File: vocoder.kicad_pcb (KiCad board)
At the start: 2 copper layers, 49.7 x 38.4 mm, 63 parts, among them J1 AudioJack4, J2 Conn_01x02_Socket, J3 Conn_01x02_Pin, J4 USB_C_Receptacle_USB2.0_16P, Q1 Q_NPN_BCE, Q2 Q_NPN_BCE, Q3 AO3401A, Q4 Q_NPN_BCE, SW1 SW_SPDT, SW2 SW_Push, SW3 SW_Push, U1 ESP32-S3-MINI-1, U3 BQ24074RGT, U4 TPS63031DSK, U5 ADAU1761

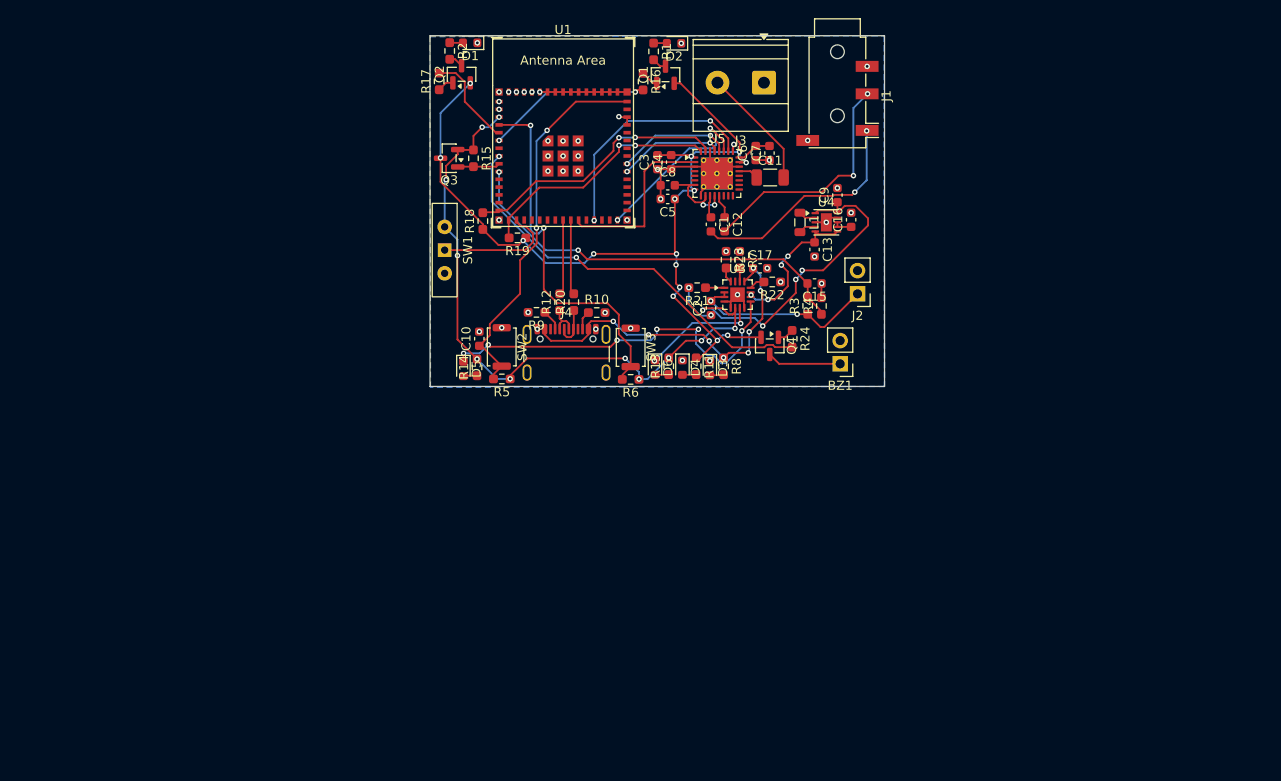
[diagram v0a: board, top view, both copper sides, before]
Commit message: replaced esp32-s3 mini with esp32-s3-wroom, added needed op amp and amp
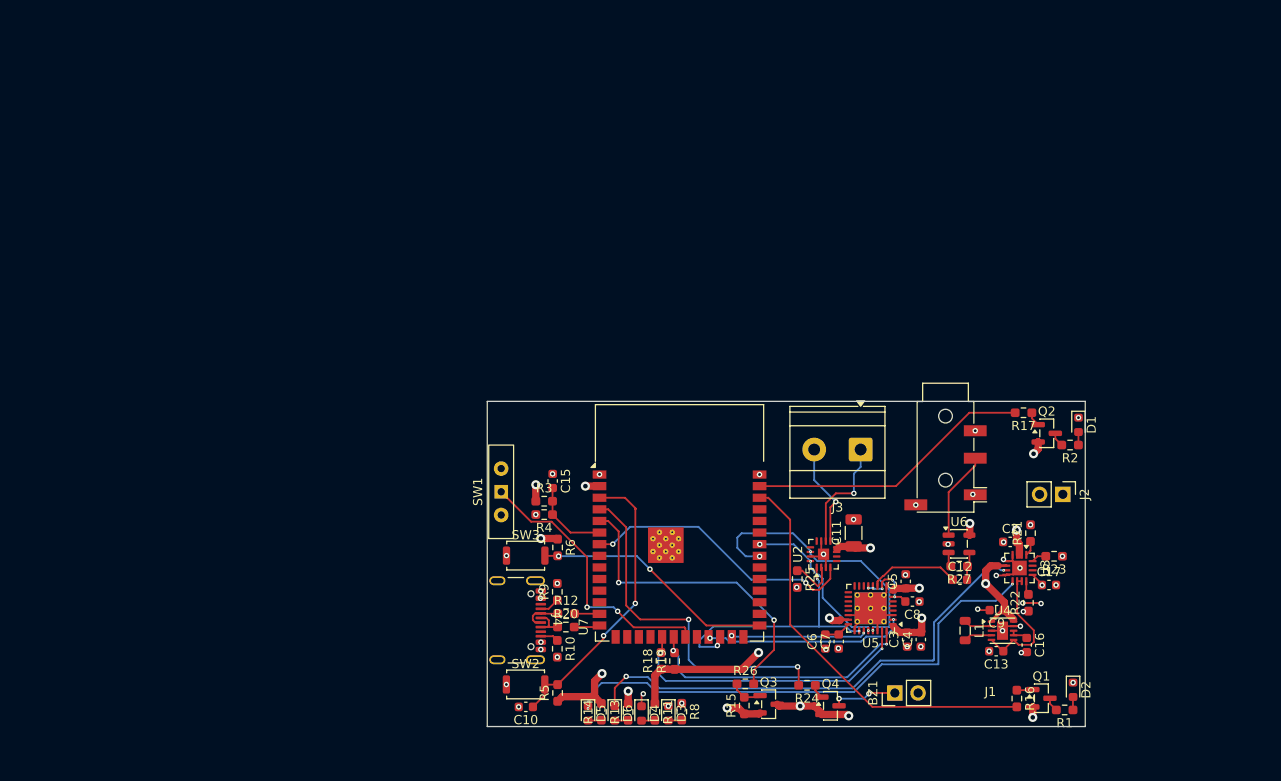
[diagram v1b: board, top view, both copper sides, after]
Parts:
- removed C1: 2.2u, Capacitor_SMD:C_0603_1608Metric
- removed R7: 72k, Resistor_SMD:R_0603_1608Metric_Pad0.98x0.95mm_HandSolder
- removed U1: ESP32-S3-MINI-1, PCM_Espressif:ESP32-S3-MINI-1
- added R25: 100k, Resistor_SMD:R_0603_1608Metric_Pad0.98x0.95mm_HandSolder, F.Cu at (156.9, 86.2)
- added R26: 100, Resistor_SMD:R_0603_1608Metric_Pad0.98x0.95mm_HandSolder, F.Cu at (151.2, 97.7)
- added R27: 51, Resistor_SMD:R_0603_1608Metric_Pad0.98x0.95mm_HandSolder, F.Cu at (174.6, 84.8)
- added U2: MAX98357A, Package_DFN_QFN:TQFN-16-1EP_3x3mm_P0.5mm_EP1.23x1.23mm, F.Cu at (159.8, 83.5)
- added U6: ~, custom_footprints:TLV9041, F.Cu at (174.6, 82.4)
- added U7: ESP32-S3-WROOM-1, RF_Module:ESP32-S3-WROOM-1, F.Cu at (144.0, 80.0)
- C11: value 10u -> 220u
- R1, R2: value 100 -> 1k
- R11, R8: value 220 -> 1k
- R18, R19: value 4.7k -> 10k
- R22, R23: value 910 -> 1k
- moved R1 84.9 mm to (186.1, 100.5), turned to 180 degrees
- moved D2 83.1 mm to (187.1, 98.3), turned to -90 degrees
- moved R2 80.4 mm to (186.7, 71.6), turned to 180 degrees
- moved Q1 79.6 mm to (183.6, 99.2), turned to 0 degrees
- moved R16 78.9 mm to (180.9, 99.3)
- moved D1 78.6 mm to (187.7, 69.3), turned to -90 degrees
- moved Q2 75.1 mm to (184.2, 70.3), turned to 0 degrees
- moved R17 73.5 mm to (181.6, 68.0), turned to 180 degrees
- moved Q3 69.2 mm to (153.8, 99.9), turned to 0 degrees
- moved R15 66.8 mm to (151.1, 100.0), turned to 90 degrees
- moved C3 58.9 mm to (168.9, 92.8)
- moved C4 58.9 mm to (170.4, 92.8)
- moved C6 54.0 mm to (160.0, 93.0)
- moved C7 54.0 mm to (161.4, 93.0)
- moved C8 52.8 mm to (169.5, 88.7), turned to 180 degrees
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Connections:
- net 3V3_SWITCH renamed Net-(Q3-G)
- C11 pad 1: Net-(U5-MONOOUT) -> BATT+
- C11 pad 2: Net-(J3-Pin_2) -> GND
- C12 pad 1: Net-(U5-RINN) -> Net-(U5-LINN)
- J1 pad R1: Net-(C12-Pad2) -> Net-(U6-+)
- J1 pad T: Net-(C1-Pad2) -> GND
- J3 pad 1: GND -> Net-(J3-Pin_1)
- Q3 pad 2: 3V3_PRE -> 3V3
- Q3 pad 3: 3V3 -> 3V3_PRE
- U3 pad 14: Net-(U3-TMR) -> unconnected-(U3-TMR-Pad14)
- U5 pad 13: Net-(U5-RINN) -> CM
- U5 pad 21: Net-(U5-MONOOUT) -> unconnected-(U5-MONOOUT-Pad21)
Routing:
- net BATT+: track 20.9 -> 73.9 mm, vias 2 -> 3
- net USB_5V: track 39.0 -> 88.1 mm, vias 8 -> 6
- net Net-(D6-K): track 13.0 -> 53.8 mm
- net 3V3_PRE: track 106.0 -> 145.5 mm, vias 15 -> 6
- net BATT_READ: track 44.9 -> 8.86 mm, vias 2 -> 0
- net 3V3: track 99.7 -> 135.1 mm, vias 15 -> 9
- net 3V3_SWITCH: track 0.00 -> 34.7 mm, vias 0 -> 2
- net AMP_SWITCH: track 0.00 -> 30.6 mm, vias 0 -> 2
- net LED_RIGHT: track 18.0 -> 44.3 mm, vias 2 -> 0
- net Net-(C1-Pad2): track 25.4 -> 0.00 mm, vias 2 -> 0
- net Net-(C12-Pad2): track 26.2 -> 3.09 mm, vias 2 -> 0
- net LED_LEFT: track 10.5 -> 31.3 mm
- net I2S_LRCLK: track 11.5 -> 29.9 mm, vias 2 -> 3
- net SWITCH_INPUT: track 13.5 -> 30.5 mm, vias 0 -> 2
- net Net-(D5-K): track 41.9 -> 56.8 mm, vias 6 -> 2
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- added copper zone on In1.Cu, net GND
- removed copper zone on B.Cu, net GND
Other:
- board size 49.7 x 38.4 mm -> 65.4 x 35.6 mm
- copper layers 2 -> 4

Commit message: semi working before removing battery and adding necessary changes
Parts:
- removed BZ1: Buzzer, Connector_PinHeader_2.54mm:PinHeader_1x02_P2.54mm_Vertical
- removed C11: 220u, Capacitor_SMD:C_1206_3216Metric
- removed C12: 2.2u, Capacitor_SMD:C_0603_1608Metric
- removed C13, C17, C9: 10u, Capacitor_SMD:C_0603_1608Metric
- removed C15: 100n, Capacitor_SMD:C_0603_1608Metric
- removed C16: 0.1u, Capacitor_SMD:C_0603_1608Metric
- removed D2: LED RED, LED_SMD:LED_0603_1608Metric
- removed J3: Conn_01x02_Pin, TerminalBlock_Phoenix:TerminalBlock_Phoenix_MKDS-1,5-2-5.08_1x02_P5.08mm_Horizontal
- removed L1: 1.5uH, Inductor_SMD:L_0805_2012Metric
- removed Q1, Q2, Q4: Q_NPN_BCE, Package_TO_SOT_SMD:SOT-23
- removed R18, R19: 10k, Resistor_SMD:R_0603_1608Metric_Pad0.98x0.95mm_HandSolder
- removed R22, R24: 1k, Resistor_SMD:R_0603_1608Metric_Pad0.98x0.95mm_HandSolder
- removed R25: 100k, Resistor_SMD:R_0603_1608Metric_Pad0.98x0.95mm_HandSolder
- removed R26: 100, Resistor_SMD:R_0603_1608Metric_Pad0.98x0.95mm_HandSolder
- removed R27: 51, Resistor_SMD:R_0603_1608Metric_Pad0.98x0.95mm_HandSolder
- removed U5: ADAU1761, Package_CSP:LFCSP-32-1EP_5x5mm_P0.5mm_EP3.5x3.5mm_ThermalVias
- removed U6: ~, custom_footprints:TLV9041
- added C1: 1u, Capacitor_SMD:C_0603_1608Metric, F.Cu at (169.6, 101.6)
- added J5: Conn_02x03_Top_Bottom, Connector_PinHeader_2.54mm:PinHeader_2x03_P2.54mm_Vertical, F.Cu at (205.5, 90.0)
- added LS1: Speaker, TerminalBlock_Phoenix:TerminalBlock_Phoenix_MKDS-1,5-2-5.08_1x02_P5.08mm_Horizontal, F.Cu at (194.2, 76.8)
- added R7: 10k, Resistor_SMD:R_0603_1608Metric_Pad0.98x0.95mm_HandSolder, F.Cu at (160.9, 82.4)
- added SW4: RotaryEncoder_Switch, Rotary_Encoder:RotaryEncoder_Bourns_Horizontal_PEC12R-2x17F-Sxxxx, F.Cu at (202.7, 100.2)
- added U1: MCP73831-2-MC, Package_DFN_QFN:DFN-8-1EP_3x2mm_P0.5mm_EP1.7x1.4mm, F.Cu at (177.9, 98.8)
- C2, C8: value 10u -> 1u
- C3, C6: value 100n -> 1u
- C4, C7: footprint Capacitor_SMD:C_0603_1608Metric -> Capacitor_SMD:C_0805_2012Metric
- C5: value 100n -> 10u; footprint Capacitor_SMD:C_0603_1608Metric -> Capacitor_SMD:C_0805_2012Metric
- D1: value LED RED -> SS34; footprint LED_SMD:LED_0603_1608Metric -> Diode_SMD:D_SOD-123
- D3: value LED BLUE -> SS34; footprint LED_SMD:LED_0603_1608Metric -> Diode_SMD:D_SOD-123
- D4: value LED GREEN -> SS34; footprint LED_SMD:LED_0603_1608Metric -> Diode_SMD:D_SOD-123
- D5: value LED RED -> 1N4148; footprint LED_SMD:LED_0603_1608Metric -> Diode_SMD:D_SOD-323
- D6: value LED GREEN -> 1N4148; footprint LED_SMD:LED_0603_1608Metric -> Diode_SMD:D_SOD-323
- J1: value AudioJack4 -> Micro_SD_Card_Det1; footprint Connector_Audio:Jack_3.5mm_PJ320D_Horizontal -> MyAntenna_manufacturer:Untitled
- R1, R11, R13, R14, R16, R17, R23, R8: value 1k -> 10k
- R2: value 1k -> 2.2k
- R3, R4: value 100k -> 470k
- SW1: value SW_SPDT -> SW_Push; footprint Button_Switch_THT:SW_Slide-03_Wuerth-WS-SLTV_10x2.5x6.4_P2.54mm -> Button_Switch_SMD:Panasonic_EVQPUJ_EVQPUA
- SW2, SW3: footprint Button_Switch_SMD:SW_Push_SPST_NO_Alps_SKRK -> Button_Switch_SMD:SW_SPST_TS-1088-xR020
- U2: value MAX98357A -> AP2112K-3.3; footprint Package_DFN_QFN:TQFN-16-1EP_3x3mm_P0.5mm_EP1.23x1.23mm -> Package_TO_SOT_SMD:SOT-23-5
- U3: value BQ24074RGT -> MAX98357A; footprint Package_DFN_QFN:VQFN-16-1EP_3x3mm_P0.5mm_EP1.6x1.6mm -> Package_DFN_QFN:TQFN-16-1EP_3x3mm_P0.5mm_EP1.23x1.23mm
- U4: value TPS63031DSK -> MAX40200AUK; footprint Package_SON:WSON-10-1EP_2.5x2.5mm_P0.5mm_EP1.2x2mm -> Package_TO_SOT_SMD:SOT-23-5
- U7: footprint RF_Module:ESP32-S3-WROOM-1 -> RF_Module:ESP32-S3-WROOM-1U
- moved SW1 78.1 mm to (202.5, 73.3), turned to 0 degrees
- moved D4 60.2 mm to (198.4, 86.7), turned to 0 degrees
- moved D3 58.0 mm to (198.4, 84.5), turned to 0 degrees
- moved D1 40.7 mm to (159.6, 98.8), turned to 180 degrees
- moved C6 35.1 mm to (194.5, 86.5), turned to -90 degrees
- moved R14 35.1 mm to (160.9, 76.5), turned to 0 degrees
- moved U7 32.1 mm to (176.1, 81.8)
- moved R13 32.0 mm to (160.9, 78.0), turned to 0 degrees
- moved R4 31.5 mm to (160.0, 86.0)
- moved R3 31.5 mm to (160.0, 84.5)
- moved R2 31.3 mm to (175.6, 100.8)
- moved R17 30.8 mm to (188.7, 98.0), turned to 0 degrees
- moved D5 29.9 mm to (163.5, 95.9)
- moved R11 28.9 mm to (160.9, 79.4), turned to 0 degrees
- moved R23 26.4 mm to (160.4, 93.3), turned to 0 degrees
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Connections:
- C2 pad 1: GND -> 3V3
- C2 pad 2: BATT+ -> GND
- C3 pad 2: 3V3 -> USB_5V
- C4 pad 1: GND -> USB_5V
- C4 pad 2: 3V3 -> GND
- C5 pad 1: 3V3 -> GND
- C5 pad 2: GND -> BATT+
- C6 pad 1: GND -> Net-(D3-K)
- C6 pad 2: Net-(U5-DVDDOUT) -> GND
- C7 pad 2: Net-(U5-DVDDOUT) -> 3V3
- C8 pad 1: GND -> 3V3
- C8 pad 2: CM -> GND
- D1 pad 1: GND -> Net-(D1-K)
- D1 pad 2: Net-(D1-A) -> USB_5V
- D3 pad 1: GND -> Net-(D3-K)
- D3 pad 2: Net-(D3-A) -> USB_5V
- D4 pad 1: GND -> Net-(D3-K)
- D4 pad 2: Net-(D4-A) -> AMP_POWER
- D5 pad 1: Net-(D5-K) -> POWER_SWITCH
- D6 pad 1: Net-(D6-K) -> BUTTON_READ
- D6 pad 2: Net-(D6-A) -> Net-(D5-A)
- Q3 pad 1: Net-(Q3-G) -> Net-(D5-A)
- Q3 pad 2: 3V3 -> Net-(D1-K)
- Q3 pad 3: 3V3_PRE -> AMP_POWER
- R1 pad 1: Net-(D2-A) -> AMP_SWITCH
- R1 pad 2: Net-(Q1-E) -> GND
- R11 pad 2: Net-(D4-A) -> CMD
- R13 pad 1: Net-(D6-A) -> 3V3
- R13 pad 2: 3V3_PRE -> D0
- R14 pad 1: Net-(D5-A) -> 3V3
- R14 pad 2: 3V3_PRE -> D1
- R15 pad 1: 3V3_PRE -> Net-(D5-A)
- R15 pad 2: Net-(Q3-G) -> Net-(D1-K)
- R16 pad 1: Net-(Q1-B) -> 3V3
- R16 pad 2: LED_RIGHT -> ENC_LEFT
- R17 pad 1: Net-(Q2-B) -> 3V3
- R17 pad 2: LED_LEFT -> ENC_RIGHT
- R2 pad 1: Net-(D1-A) -> Net-(U1-PROG)
- R2 pad 2: Net-(Q2-E) -> GND
- R21 pad 1: Net-(U3-TS) -> 3V3
- R21 pad 2: GND -> ENC_PUSH
- R23 pad 1: GND -> 3V3
- R23 pad 2: Net-(U3-ISET) -> BUTTON_READ
- R5 pad 1: 3V3_PRE -> 3V3
- R6 pad 1: 3V3_PRE -> 3V3
- R8 pad 1: USB_5V -> 3V3
- R8 pad 2: Net-(D3-A) -> D3
- SW1 pad 1: SWITCH_INPUT -> BUTTON_READ
- SW1 pad 2: 3V3_PRE -> GND
- U2 pad 1: I2S_DATA_OUT -> AMP_POWER
- U2 pad 2: Net-(U2-GAIN_SLOT) -> GND
- U2 pad 3: GND -> AMP_POWER
- U2 pad 4: AMP_SWITCH -> unconnected-(U2-NC-Pad4)
- U2 pad 5: unconnected-(U2-NC-Pad5) -> 3V3
- U3 pad 1: Net-(U3-TS) -> I2S_DATA_OUT
- U3 pad 10: Net-(U4-EN) -> Net-(U3-OUTN)
- U3 pad 11: Net-(U4-EN) -> GND
- U3 pad 12: Net-(U3-ILIM) -> unconnected-(U3-NC-Pad12)
- U3 pad 13: USB_5V -> unconnected-(U3-NC-Pad13)
- U3 pad 14: unconnected-(U3-TMR-Pad14) -> I2S_LRCLK
- U3 pad 15: unconnected-(U3-ITERM-Pad15) -> GND
- U3 pad 16: Net-(U3-ISET) -> I2S_BCLK
- U3 pad 2: BATT+ -> GND
- U3 pad 3: BATT+ -> GND
- U3 pad 4: GND -> AMP_SWITCH
- U3 pad 5: GND -> unconnected-(U3-NC-Pad5)
- U3 pad 6: 3V3_PRE -> unconnected-(U3-NC-Pad6)
- U3 pad 7: Net-(D6-K) -> Net-(D3-K)
- U3 pad 8: GND -> Net-(D3-K)
- U3 pad 9: Net-(D5-K) -> Net-(U3-OUTP)
- U4 pad 1: 3V3_PRE -> BATT+
- U4 pad 2: Net-(U4-L2) -> GND
- U4 pad 3: GND -> BATT+
- U4 pad 4: Net-(U4-L1) -> unconnected-(U4-NC-Pad4)
- U4 pad 5: Net-(U4-EN) -> Net-(D1-K)
- U7 pad 10: unconnected-(U7-IO17-Pad10) -> BATT_READ
- U7 pad 11: unconnected-(U7-IO18-Pad11) -> POWER_SWITCH
- U7 pad 19: SDA -> CHARGE_STATUS
- U7 pad 2: 3V3_PRE -> 3V3
- U7 pad 20: SCL -> unconnected-(U7-IO12-Pad20)
- U7 pad 21: SWITCH_INPUT -> BUTTON_READ
- U7 pad 22: unconnected-(U7-IO14-Pad22) -> DET
- U7 pad 23: I2S_MCLK -> ENC_LEFT
- U7 pad 24: I2S_DATA_OUT -> ENC_PUSH
- U7 pad 25: I2S_DATA_IN -> ENC_RIGHT
- U7 pad 31: unconnected-(U7-IO38-Pad31) -> AMP_SWITCH
- U7 pad 32: unconnected-(U7-IO39-Pad32) -> I2S_DATA_OUT
- U7 pad 33: I2S_LRCLK -> I2S_BCLK
- U7 pad 34: I2S_BCLK -> I2S_LRCLK
- U7 pad 38: LED_RIGHT -> I2S_MCLK
- U7 pad 39: LED_LEFT -> I2S_DATA_IN
- U7 pad 4: BUZZER -> D1
- U7 pad 5: 3V3_SWITCH -> D0
- U7 pad 6: BATT_READ -> CLK
- U7 pad 7: AMP_SWITCH -> CMD
- U7 pad 8: unconnected-(U7-IO15-Pad8) -> D3
- U7 pad 9: unconnected-(U7-IO16-Pad9) -> D2
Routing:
- net 3V3_PRE: track 145.5 -> 0.00 mm, vias 6 -> 0
- net BUTTON_READ: track 0.00 -> 69.1 mm, vias 0 -> 3
- net Net-(D5-K): track 56.8 -> 0.00 mm, vias 2 -> 0
- net Net-(D6-K): track 53.8 -> 0.00 mm, vias 2 -> 0
- net AMP_POWER: track 0.00 -> 47.7 mm, vias 0 -> 2
- net LED_RIGHT: track 44.3 -> 0.00 mm
- net BUZZER: track 38.5 -> 0.00 mm, vias 2 -> 0
- net DET: track 0.00 -> 35.2 mm, vias 0 -> 2
- net 3V3_SWITCH: track 34.7 -> 0.00 mm, vias 2 -> 0
- net SDA: track 32.4 -> 0.00 mm, vias 2 -> 0
- net ENC_LEFT: track 0.00 -> 31.9 mm
- net LED_LEFT: track 31.3 -> 0.00 mm
- net SCL: track 30.5 -> 0.00 mm, vias 2 -> 0
- net SWITCH_INPUT: track 30.5 -> 0.00 mm, vias 2 -> 0
- net ENC_RIGHT: track 0.00 -> 25.4 mm
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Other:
- board size 65.4 x 35.6 mm -> 66 x 34.8 mm

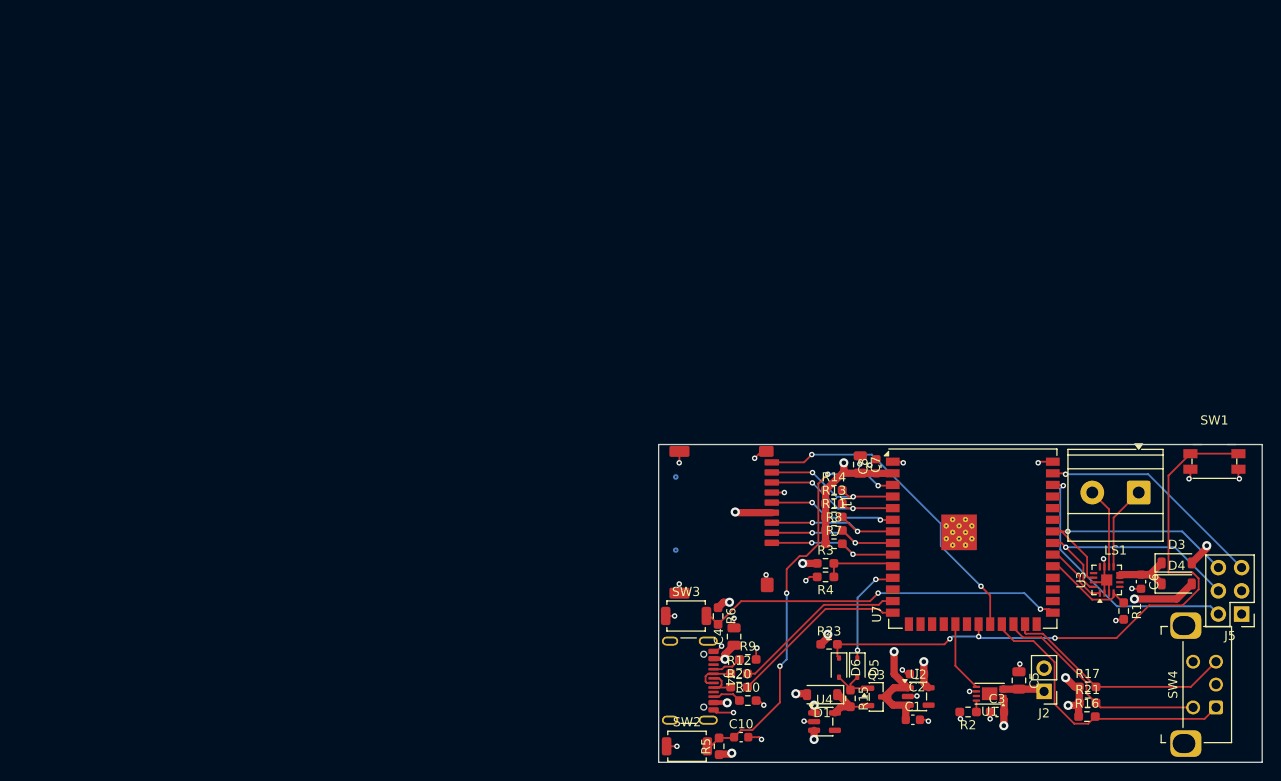
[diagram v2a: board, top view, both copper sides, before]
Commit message: reduced board size, removed BMS, will be powered externally only, fixed I2S wiring
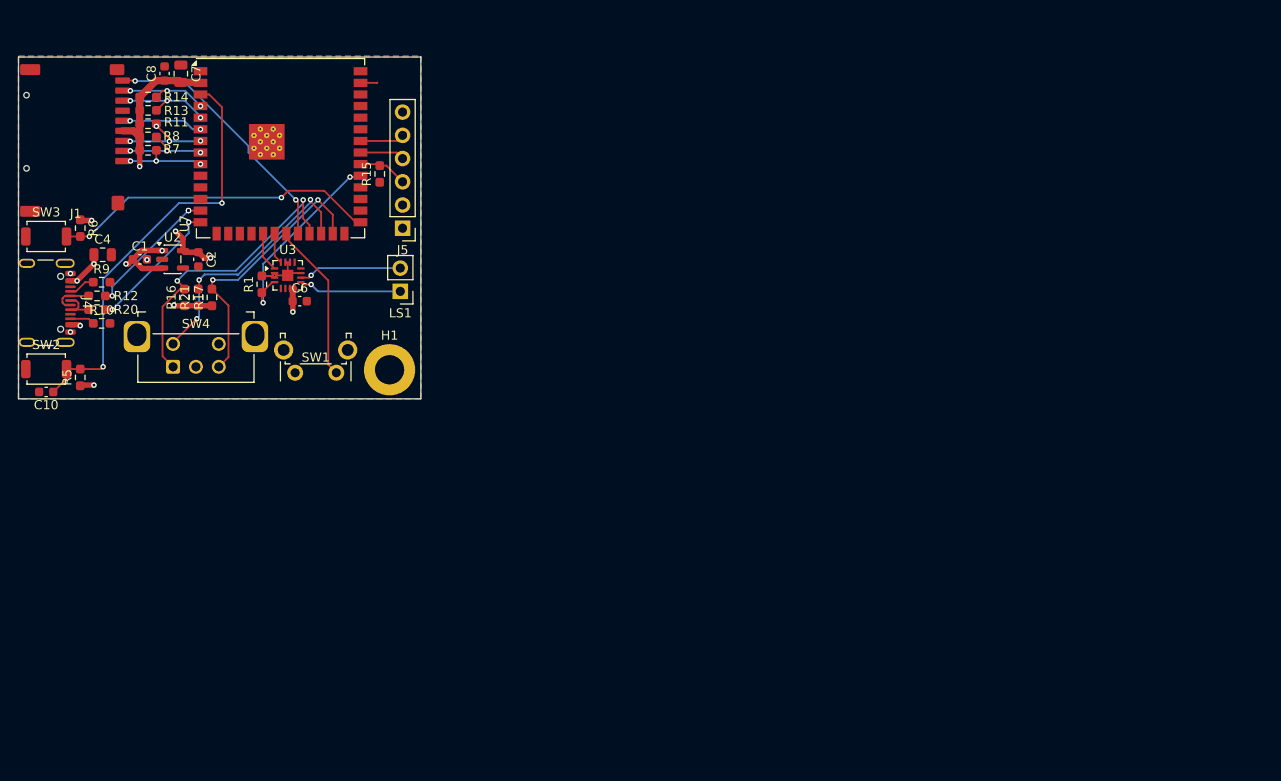
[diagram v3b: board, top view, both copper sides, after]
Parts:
- removed C3: 1u, Capacitor_SMD:C_0603_1608Metric
- removed C5: 10u, Capacitor_SMD:C_0805_2012Metric
- removed D1, D3, D4: SS34, Diode_SMD:D_SOD-123
- removed D5, D6: 1N4148, Diode_SMD:D_SOD-323
- removed J2: Conn_01x02_Socket, Connector_PinHeader_2.54mm:PinHeader_1x02_P2.54mm_Vertical
- removed Q3: AO3401A, Package_TO_SOT_SMD:SOT-23
- removed R2: 2.2k, Resistor_SMD:R_0603_1608Metric_Pad0.98x0.95mm_HandSolder
- removed R23: 10k, Resistor_SMD:R_0603_1608Metric_Pad0.98x0.95mm_HandSolder
- removed R3, R4: 470k, Resistor_SMD:R_0603_1608Metric_Pad0.98x0.95mm_HandSolder
- removed U1: MCP73831-2-MC, Package_DFN_QFN:DFN-8-1EP_3x2mm_P0.5mm_EP1.7x1.4mm
- removed U4: MAX40200AUK, Package_TO_SOT_SMD:SOT-23-5
- added H1: MountingHole_Pad, MountingHole:MountingHole_3.2mm_M3_DIN965_Pad, F.Cu at (112.3, 63.3)
- J5: footprint Connector_PinHeader_2.54mm:PinHeader_2x03_P2.54mm_Vertical -> Connector_PinHeader_2.54mm:PinHeader_1x06_P2.54mm_Vertical
- LS1: footprint TerminalBlock_Phoenix:TerminalBlock_Phoenix_MKDS-1,5-2-5.08_1x02_P5.08mm_Horizontal -> Connector_PinHeader_2.54mm:PinHeader_1x02_P2.54mm_Vertical
- SW1: footprint Button_Switch_SMD:Panasonic_EVQPUJ_EVQPUA -> Button_Switch_THT:SW_Tactile_SPST_Angled_PTS645Vx58-2LFS
- moved SW4 120.0 mm to (88.7, 63.0), turned to 90 degrees
- moved R16 108.8 mm to (89.9, 55.4), turned to 90 degrees
- moved R21 106.9 mm to (91.4, 55.4), turned to 90 degrees
- moved R17 104.8 mm to (92.9, 55.4), turned to 90 degrees
- moved J5 101.0 mm to (113.8, 47.9)
- moved R1 100.8 mm to (98.4, 54.0), turned to 90 degrees
- moved C1 98.4 mm to (85.0, 51.2)
- moved C6 97.0 mm to (102.5, 55.8), turned to 0 degrees
- moved SW1 96.5 mm to (106.5, 63.6), turned to 180 degrees
- moved U3 95.6 mm to (101.2, 53.0), turned to 0 degrees
- moved U2 94.5 mm to (88.6, 51.2)
- moved C2 90.7 mm to (91.4, 51.2), turned to -90 degrees
- moved C8 88.9 mm to (87.7, 30.9)
- moved U7 86.9 mm to (100.4, 39.1)
- moved R7 86.5 mm to (85.9, 39.3)
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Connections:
- C1 pad 1: AMP_POWER -> USB_5V
- C6 pad 1: Net-(D3-K) -> USB_5V
- J5 pad 1: 3V3 -> GND
- J5 pad 2: I2S_MCLK -> 3V3
- J5 pad 3: GND -> I2S_DATA_IN
- J5 pad 4: I2S_BCLK -> I2S_BCLK_MIC
- J5 pad 5: I2S_DATA_IN -> I2S_WS
- J5 pad 6: I2S_LRCLK -> GND
- R15 pad 1: Net-(D5-A) -> GND
- R15 pad 2: Net-(D1-K) -> I2S_DATA_IN
- U2 pad 1: AMP_POWER -> USB_5V
- U2 pad 3: AMP_POWER -> USB_5V
- U3 pad 14: I2S_LRCLK -> GND
- U3 pad 16: I2S_BCLK -> I2S_BCLK_SPEAKER
- U3 pad 7: Net-(D3-K) -> USB_5V
- U3 pad 8: Net-(D3-K) -> USB_5V
- U7 pad 10: BATT_READ -> unconnected-(U7-IO17-Pad10)
- U7 pad 11: POWER_SWITCH -> unconnected-(U7-IO18-Pad11)
- U7 pad 19: CHARGE_STATUS -> I2S_DATA_OUT
- U7 pad 20: unconnected-(U7-IO12-Pad20) -> I2S_BCLK_SPEAKER
- U7 pad 32: I2S_DATA_OUT -> I2S_DATA_IN
- U7 pad 33: I2S_BCLK -> I2S_BCLK_MIC
- U7 pad 34: I2S_LRCLK -> I2S_WS
- U7 pad 38: I2S_MCLK -> unconnected-(U7-IO2-Pad38)
- U7 pad 39: I2S_DATA_IN -> unconnected-(U7-IO1-Pad39)
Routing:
- net 3V3: track 149.6 -> 93.3 mm, vias 8 -> 6
- net BATT+: track 56.2 -> 0.00 mm, vias 3 -> 0
- net BUTTON_READ: track 69.1 -> 17.5 mm, vias 3 -> 0
- net AMP_POWER: track 47.7 -> 0.00 mm, vias 2 -> 0
- net USB_5V: track 86.0 -> 43.4 mm, vias 5 -> 6
- net GND: track 41.9 -> 8.49 mm, vias 31 -> 3
- net I2S_MCLK: track 28.5 -> 0.00 mm, vias 1 -> 0
- net I2S_LRCLK: track 27.5 -> 0.00 mm, vias 1 -> 0
- net I2S_BCLK: track 26.1 -> 0.00 mm, vias 1 -> 0
- net I2S_DATA_IN: track 24.9 -> 5.40 mm, vias 1 -> 0
- net AMP_SWITCH: track 10.2 -> 21.9 mm, vias 0 -> 2
- net POWER_SWITCH: track 11.4 -> 0.00 mm, vias 2 -> 0
- net BATT_READ: track 8.05 -> 0.00 mm
- net CHARGE_STATUS: track 7.81 -> 0.00 mm
- net Net-(D3-K): track 7.81 -> 0.00 mm
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- added copper zone on B.Cu, net GND
- added copper zone on F.Cu, net GND
- added copper zone on In2.Cu, net GND
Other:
- board size 66 x 34.8 mm -> 44 x 37.4 mm
